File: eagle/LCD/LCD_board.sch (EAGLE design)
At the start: 7 parts, among them CN1 1X4-CLEANBIG

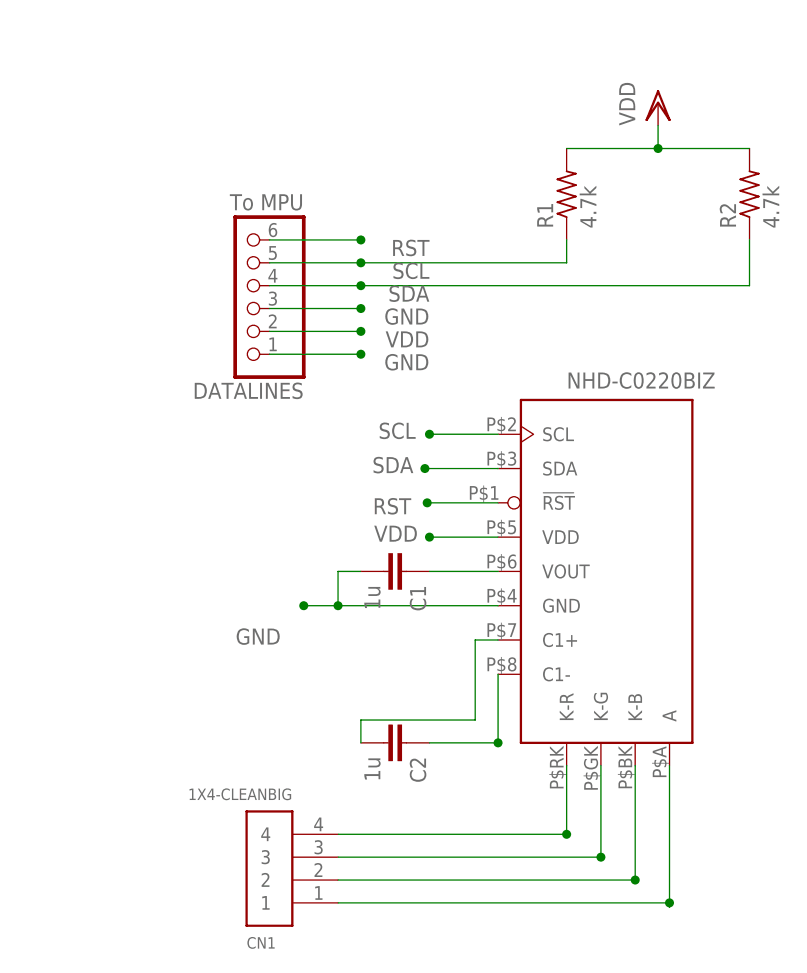
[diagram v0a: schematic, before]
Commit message: Updated LCD board with surface mount components and a 2x4 header connector
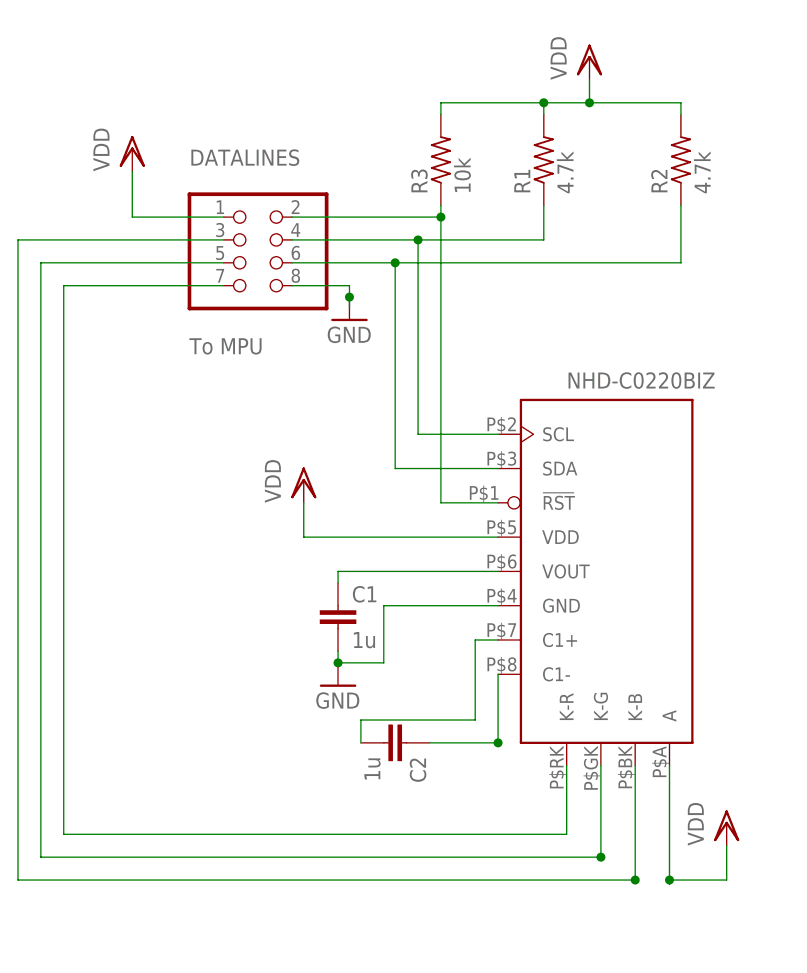
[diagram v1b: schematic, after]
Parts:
- removed CN1: 1X4-CLEANBIG, adafruit:1X4-CLEANBIG
- added R3: 10k, T06_LockBox:R-US_M0805
- C1, C2: device capacitor-wima:C15/8 -> T06_LockBox:C
- DATALINES: device adafruit:PINHD-1X6 -> T06_LockBox:PINHD-2X4
- R1, R2: device T06_LockBox:R-US_0204/5 -> T06_LockBox:R-US_M0805
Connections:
- removed net A: CN1.4, U$1.K-R
- removed net GK: CN1.2, U$1.K-B
- removed net N$2: CN1.3, U$1.K-G
- removed net N$4: CN1.1, U$1.A
- removed net RST: DATALINES.6, U$1.!RST
- new net K-B: DATALINES.3, U$1.K-B
- new net K-G: DATALINES.5, U$1.K-G
- new net K-R: DATALINES.7, U$1.K-R
- new net N$6: DATALINES.2, R3.1, U$1.!RST
- net GND: now also DATALINES.8; no longer DATALINES.1, DATALINES.3
- net SCL: now also DATALINES.4; no longer DATALINES.5
- net SDA: now also DATALINES.6; no longer DATALINES.4
- net VDD: now also DATALINES.1, R3.2, U$1.A; no longer DATALINES.2
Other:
- moved on the sheet: C1, R1, R2

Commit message: Created 2 layer LDC board with smaller footprint than previous versions
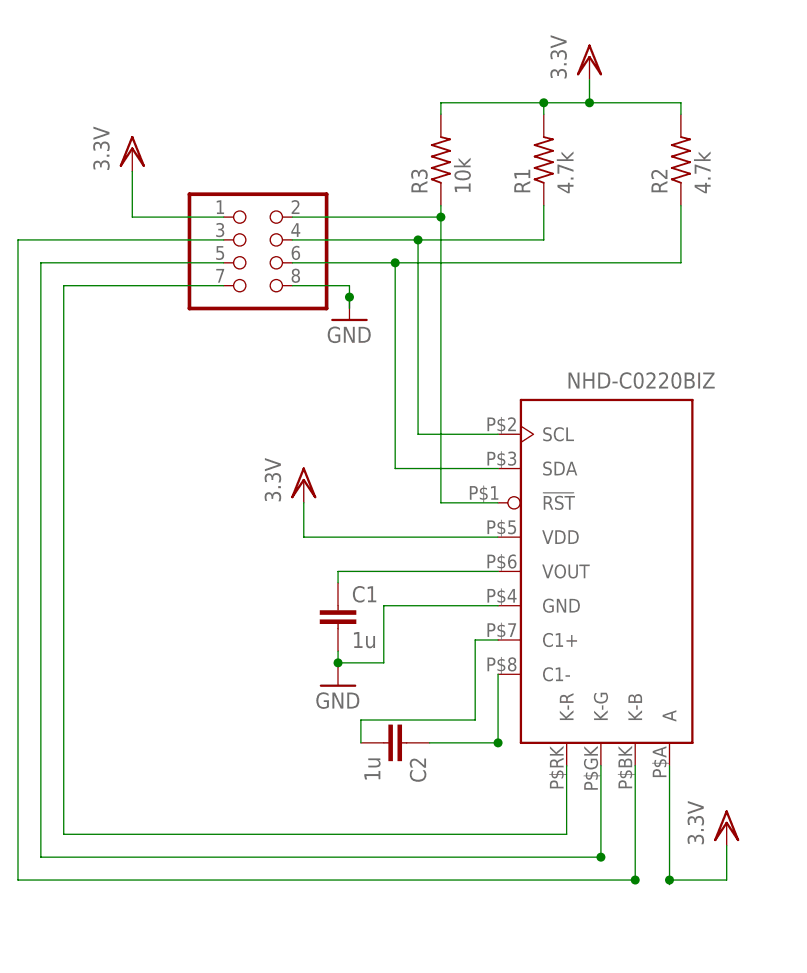
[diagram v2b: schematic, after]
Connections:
- net K-B renamed EN_BL
- net K-G renamed EN_G
- net K-R renamed EN_RD
- net N$6 renamed !LCD_RST
- net VDD renamed 3.3V
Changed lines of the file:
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@@
 <setting verticaltext="up"/>
 </settings>
-<grid distance="0.05" unitdist="inch" unit="inch" style="lines" multiple="1" display="yes" altdistance="0.01" altunitdist="inch" altunit="inch"/>
+<grid distance="0.1" unitdist="inch" unit="inch" style="lines" multiple="1" display="no" altdistance="0.01" altunitdist="inch" altunit="inch"/>
 <layers>
 <layer number="1" name="Top" color="4" fill="1" visible="no" active="no"/>
@@
 <part name="R1" library="T06_LockBox" deviceset="R-US_" device="M0805" value="4.7k"/>
 <part name="R2" library="T06_LockBox" deviceset="R-US_" device="M0805" value="4.7k"/>
-<part name="VDD1" library="supply1" deviceset="VDD" device=""/>
+<part name="VDD1" library="supply1" deviceset="VDD" device="" value="3.3V"/>
 <part name="U$1" library="T06_LockBox" deviceset="NHD-C0220BIZ" device=""/>
 <part name="GND1" library="T06_LockBox" deviceset="GND" device=""/>
 <part name="GND2" library="T06_LockBox" deviceset="GND" device=""/>
-<part name="VDD2" library="supply1" deviceset="VDD" device=""/>
-<part name="VDD3" library="supply1" deviceset="VDD" device=""/>
-<part name="VDD4" library="supply1" deviceset="VDD" device=""/>
+<part name="VDD2" library="supply1" deviceset="VDD" device="" value="3.3V"/>
+<part name="VDD3" library="supply1" deviceset="VDD" device="" value="3.3V"/>
+<part name="VDD4" library="supply1" deviceset="VDD" device="" value="3.3V"/>
 <part name="R3" library="T06_LockBox" deviceset="R-US_" device="M0805" value="10k"/>
 </parts>
@@
 <instances>
 <instance part="DATALINES" gate="A" x="63.5" y="66.04" smashed="yes">
-<attribute name="NAME" x="57.15" y="76.835" size="1.778" layer="95"/>
-<attribute name="VALUE" x="57.15" y="55.88" size="1.778" layer="96"/>
 <attribute name="DATALINES" x="63.5" y="66.04" size="1.778" layer="96" display="off"/>
 </instance>
@@
 </segment>
 </net>
-<net name="VDD" class="0">
+<net name="EN_BL" class="0">
+<segment>
+<wire x1="106.68" y1="10.16" x2="106.68" y2="-2.54" width="0.1524" layer="91"/>
+<wire x1="106.68" y1="-2.54" x2="38.1" y2="-2.54" width="0.1524" layer="91"/>
+<junction x="106.68" y="-2.54"/>
+<pinref part="U$1" gate="G$1" pin="K-B"/>
+<pinref part="DATALINES" gate="A" pin="3"/>
+<wire x1="60.96" y1="68.58" x2="38.1" y2="68.58" width="0.1524" layer="91"/>
+<wire x1="38.1" y1="68.58" x2="38.1" y2="-2.54" width="0.1524" layer="91"/>
+</segment>
+</net>
+<net name="EN_G" class="0">
+<segment>
+<wire x1="102.87" y1="10.16" x2="102.87" y2="0" width="0.1524" layer="91"/>
+<wire x1="102.87" y1="-0.254" x2="102.87" y2="0" width="0.1524" layer="91"/>
+<junction x="102.87" y="0"/>
+<pinref part="U$1" gate="G$1" pin="K-G"/>
+<pinref part="DATALINES" gate="A" pin="5"/>
+<wire x1="60.96" y1="66.04" x2="40.64" y2="66.04" width="0.1524" layer="91"/>
+<wire x1="40.64" y1="66.04" x2="40.64" y2="0" width="0.1524" layer="91"/>
+<wire x1="40.64" y1="0" x2="102.87" y2="0" width="0.1524" layer="91"/>
+</segment>
+</net>
+<net name="!LCD_RST" class="0">
+<segment>
+<pinref part="U$1" gate="G$1" pin="!RST"/>
+<wire x1="91.44" y1="39.37" x2="85.09" y2="39.37" width="0.1524" layer="91"/>
+<wire x1="85.09" y1="39.37" x2="85.09" y2="71.12" width="0.1524" layer="91"/>
+<pinref part="DATALINES" gate="A" pin="2"/>
+<wire x1="85.09" y1="71.12" x2="68.58" y2="71.12" width="0.1524" layer="91"/>
+<pinref part="R3" gate="G$1" pin="1"/>
+<wire x1="85.09" y1="71.12" x2="85.09" y2="72.39" width="0.1524" layer="91"/>
+<junction x="85.09" y="71.12"/>
+</segment>
+</net>
+<net name="N$5" class="0">
+<segment>
+<pinref part="U$1" gate="G$1" pin="VOUT"/>
+<wire x1="91.44" y1="31.75" x2="73.66" y2="31.75" width="0.1524" layer="91"/>
+<pinref part="C1" gate="G$1" pin="1"/>
+<wire x1="73.66" y1="31.75" x2="73.66" y2="30.48" width="0.1524" layer="91"/>
+</segment>
+</net>
+<net name="GND" class="0">
+<segment>
+<pinref part="C1" gate="G$1" pin="2"/>
+<pinref part="GND1" gate="1" pin="GND"/>
+<wire x1="73.66" y1="22.86" x2="73.66" y2="21.59" width="0.1524" layer="91"/>
+<pinref part="U$1" gate="G$1" pin="GND"/>
+<wire x1="91.44" y1="27.94" x2="78.74" y2="27.94" width="0.1524" layer="91"/>
+<wire x1="78.74" y1="27.94" x2="78.74" y2="21.59" width="0.1524" layer="91"/>
+<wire x1="78.74" y1="21.59" x2="73.66" y2="21.59" width="0.1524" layer="91"/>
+<junction x="73.66" y="21.59"/>
+</segment>
+<segment>
+<pinref part="DATALINES" gate="A" pin="8"/>
+<wire x1="68.58" y1="63.5" x2="74.93" y2="63.5" width="0.1524" layer="91"/>
+<wire x1="74.93" y1="63.5" x2="74.93" y2="62.23" width="0.1524" layer="91"/>
+<pinref part="GND2" gate="1" pin="GND"/>
+<wire x1="74.93" y1="62.23" x2="74.93" y2="60.96" width="0.1524" layer="91"/>
+<junction x="74.93" y="62.23"/>
+</segment>
+</net>
+<net name="EN_RD" class="0">
+<segment>
+<pinref part="DATALINES" gate="A" pin="7"/>
+<wire x1="60.96" y1="63.5" x2="43.18" y2="63.5" width="0.1524" layer="91"/>
+<wire x1="43.18" y1="63.5" x2="43.18" y2="2.54" width="0.1524" layer="91"/>
+<wire x1="43.18" y1="2.54" x2="99.06" y2="2.54" width="0.1524" layer="91"/>
+<pinref part="U$1" gate="G$1" pin="K-R"/>
+<wire x1="99.06" y1="2.54" x2="99.06" y2="10.16" width="0.1524" layer="91"/>
+</segment>
+</net>
+<net name="3.3V" class="0">
+<segment>
+<pinref part="DATALINES" gate="A" pin="1"/>
+<wire x1="60.96" y1="71.12" x2="50.8" y2="71.12" width="0.1524" layer="91"/>
+<wire x1="50.8" y1="71.12" x2="50.8" y2="76.2" width="0.1524" layer="91"/>
+<pinref part="VDD2" gate="G$1" pin="VDD"/>
+</segment>
 <segment>
 <pinref part="R1" gate="G$1" pin="2"/>
@@
 </segment>
 <segment>
-<pinref part="DATALINES" gate="A" pin="1"/>
-<wire x1="60.96" y1="71.12" x2="50.8" y2="71.12" width="0.1524" layer="91"/>
-<wire x1="50.8" y1="71.12" x2="50.8" y2="76.2" width="0.1524" layer="91"/>
-<pinref part="VDD2" gate="G$1" pin="VDD"/>
-</segment>
-<segment>
 <wire x1="110.49" y1="10.16" x2="110.49" y2="-2.54" width="0.1524" layer="91"/>
 <pinref part="U$1" gate="G$1" pin="A"/>
@@
 </segment>
 </net>
-<net name="K-B" class="0">
-<segment>
-<wire x1="106.68" y1="10.16" x2="106.68" y2="-2.54" width="0.1524" layer="91"/>
-<wire x1="106.68" y1="-2.54" x2="38.1" y2="-2.54" width="0.1524" layer="91"/>
-<junction x="106.68" y="-2.54"/>
-<pinref part="U$1" gate="G$1" pin="K-B"/>
-<pinref part="DATALINES" gate="A" pin="3"/>
-<wire x1="60.96" y1="68.58" x2="38.1" y2="68.58" width="0.1524" layer="91"/>
-<wire x1="38.1" y1="68.58" x2="38.1" y2="-2.54" width="0.1524" layer="91"/>
-</segment>
-</net>
-<net name="K-G" class="0">
-<segment>
-<wire x1="102.87" y1="10.16" x2="102.87" y2="0" width="0.1524" layer="91"/>
-<wire x1="102.87" y1="-0.254" x2="102.87" y2="0" width="0.1524" layer="91"/>
-<junction x="102.87" y="0"/>
-<pinref part="U$1" gate="G$1" pin="K-G"/>
-<pinref part="DATALINES" gate="A" pin="5"/>
-<wire x1="60.96" y1="66.04" x2="40.64" y2="66.04" width="0.1524" layer="91"/>
-<wire x1="40.64" y1="66.04" x2="40.64" y2="0" width="0.1524" layer="91"/>
-<wire x1="40.64" y1="0" x2="102.87" y2="0" width="0.1524" layer="91"/>
-</segment>
-</net>
-<net name="N$6" class="0">
-<segment>
-<pinref part="U$1" gate="G$1" pin="!RST"/>
-<wire x1="91.44" y1="39.37" x2="85.09" y2="39.37" width="0.1524" layer="91"/>
-<wire x1="85.09" y1="39.37" x2="85.09" y2="71.12" width="0.1524" layer="91"/>
-<pinref part="DATALINES" gate="A" pin="2"/>
-<wire x1="85.09" y1="71.12" x2="68.58" y2="71.12" width="0.1524" layer="91"/>
-<pinref part="R3" gate="G$1" pin="1"/>
-<wire x1="85.09" y1="71.12" x2="85.09" y2="72.39" width="0.1524" layer="91"/>
-<junction x="85.09" y="71.12"/>
-</segment>
-</net>
-<net name="N$5" class="0">
-<segment>
-<pinref part="U$1" gate="G$1" pin="VOUT"/>
-<wire x1="91.44" y1="31.75" x2="73.66" y2="31.75" width="0.1524" layer="91"/>
-<pinref part="C1" gate="G$1" pin="1"/>
-<wire x1="73.66" y1="31.75" x2="73.66" y2="30.48" width="0.1524" layer="91"/>
-</segment>
-</net>
-<net name="GND" class="0">
-<segment>
-<pinref part="C1" gate="G$1" pin="2"/>
-<pinref part="GND1" gate="1" pin="GND"/>
-<wire x1="73.66" y1="22.86" x2="73.66" y2="21.59" width="0.1524" layer="91"/>
-<pinref part="U$1" gate="G$1" pin="GND"/>
-<wire x1="91.44" y1="27.94" x2="78.74" y2="27.94" width="0.1524" layer="91"/>
-<wire x1="78.74" y1="27.94" x2="78.74" y2="21.59" width="0.1524" layer="91"/>
-<wire x1="78.74" y1="21.59" x2="73.66" y2="21.59" width="0.1524" layer="91"/>
-<junction x="73.66" y="21.59"/>
-</segment>
-<segment>
-<pinref part="DATALINES" gate="A" pin="8"/>
-<wire x1="68.58" y1="63.5" x2="74.93" y2="63.5" width="0.1524" layer="91"/>
-<wire x1="74.93" y1="63.5" x2="74.93" y2="62.23" width="0.1524" layer="91"/>
-<pinref part="GND2" gate="1" pin="GND"/>
-<wire x1="74.93" y1="62.23" x2="74.93" y2="60.96" width="0.1524" layer="91"/>
-<junction x="74.93" y="62.23"/>
-</segment>
-</net>
-<net name="K-R" class="0">
-<segment>
-<pinref part="DATALINES" gate="A" pin="7"/>
-<wire x1="60.96" y1="63.5" x2="43.18" y2="63.5" width="0.1524" layer="91"/>
-<wire x1="43.18" y1="63.5" x2="43.18" y2="2.54" width="0.1524" layer="91"/>
-<wire x1="43.18" y1="2.54" x2="99.06" y2="2.54" width="0.1524" layer="91"/>
-<pinref part="U$1" gate="G$1" pin="K-R"/>
-<wire x1="99.06" y1="2.54" x2="99.06" y2="10.16" width="0.1524" layer="91"/>
-</segment>
-</net>
